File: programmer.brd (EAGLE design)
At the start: 45.7 x 20.3 mm, 23 parts, among them IC1 74241, U1 ATMEGA8U2, X2 SPARKFUN_USB-MICROB, Y1 16MHz

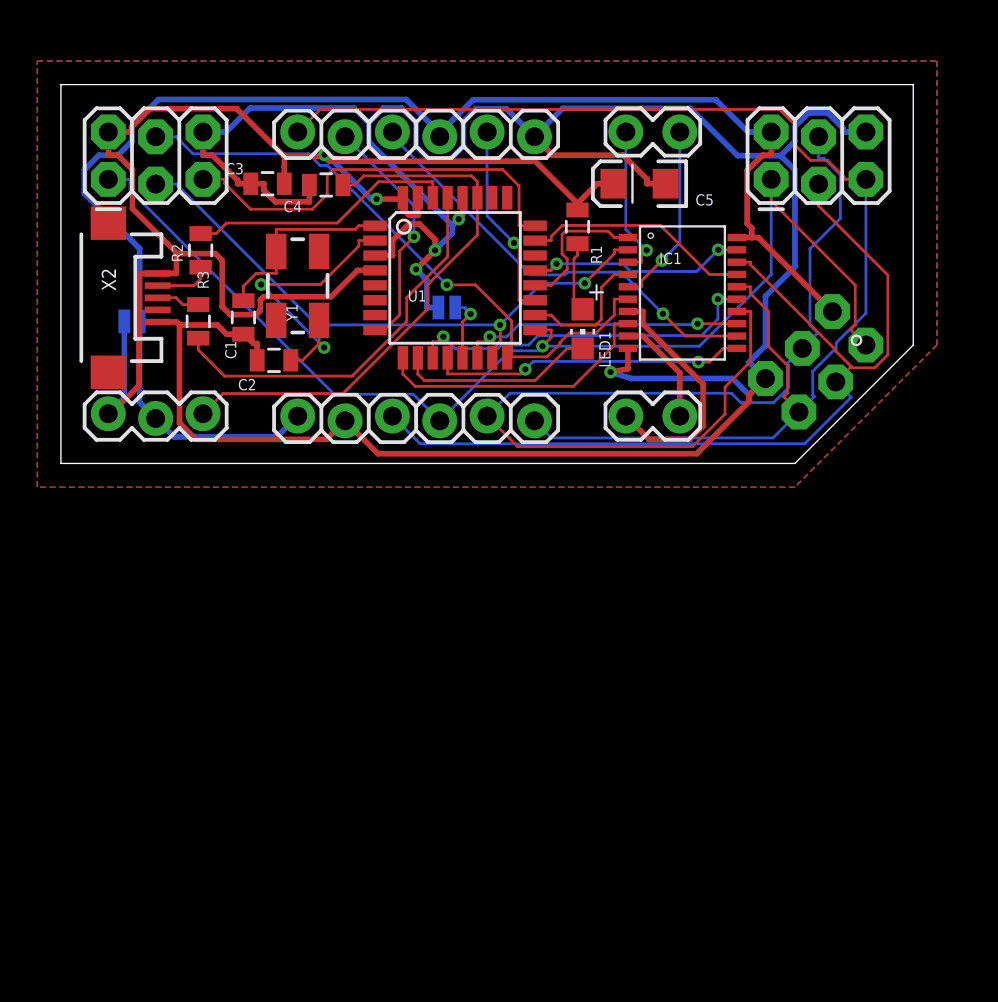
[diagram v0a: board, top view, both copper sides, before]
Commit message: Added gratuitous ground plane vias for more complete coverage.  There was already one (routing, not ground plane) via in a slightly bottom silk-obscuring place, but this change doesn't add any more.
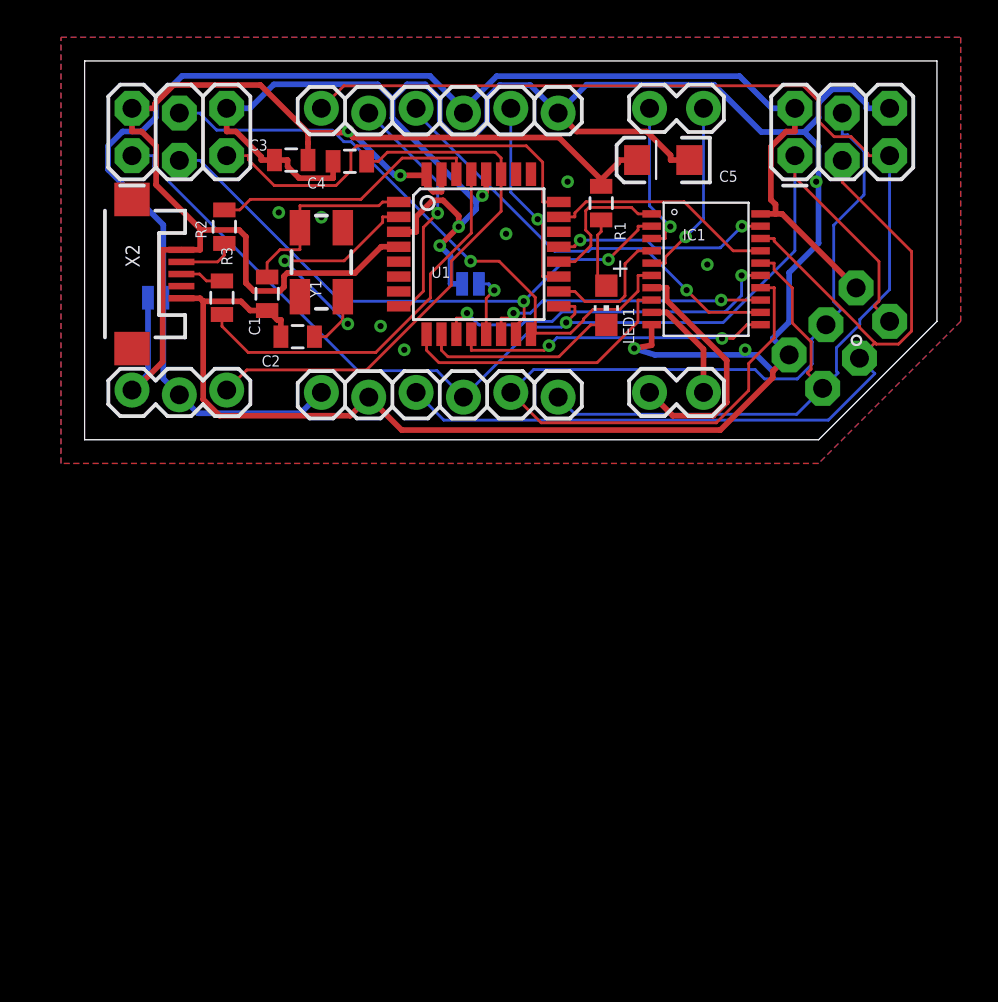
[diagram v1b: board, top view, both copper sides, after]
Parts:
- moved IC1 1.80 mm to (33.4, 9.42)
- moved ISP 1.80 mm to (38.1, 15.2)
- moved ISP-RA 1.80 mm to (43.2, 6.35)
- moved SJ1 1.80 mm to (3.81, 7.62)
- moved X2 1.80 mm to (2.54, 8.89)
- moved JP1 1.80 mm to (2.54, 2.54)
- moved C1 1.80 mm to (9.79, 7.83)
- moved C2 1.80 mm to (11.4, 5.53)
- moved ISP-SELF 1.80 mm to (2.54, 15.2)
- moved JP2 1.80 mm to (12.7, 2.54)
- moved JP5 1.80 mm to (30.5, 2.54)
- moved R2 1.80 mm to (7.49, 11.4)
- moved R3 1.80 mm to (7.37, 7.62)
- moved SJ2 1.80 mm to (20.7, 8.36)
- moved C3 1.80 mm to (11.1, 15.0)
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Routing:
- net GND: vias 4 -> 13

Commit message: Passes design rules now.  More gratuitous ground plane vias, none of which obscure silk.
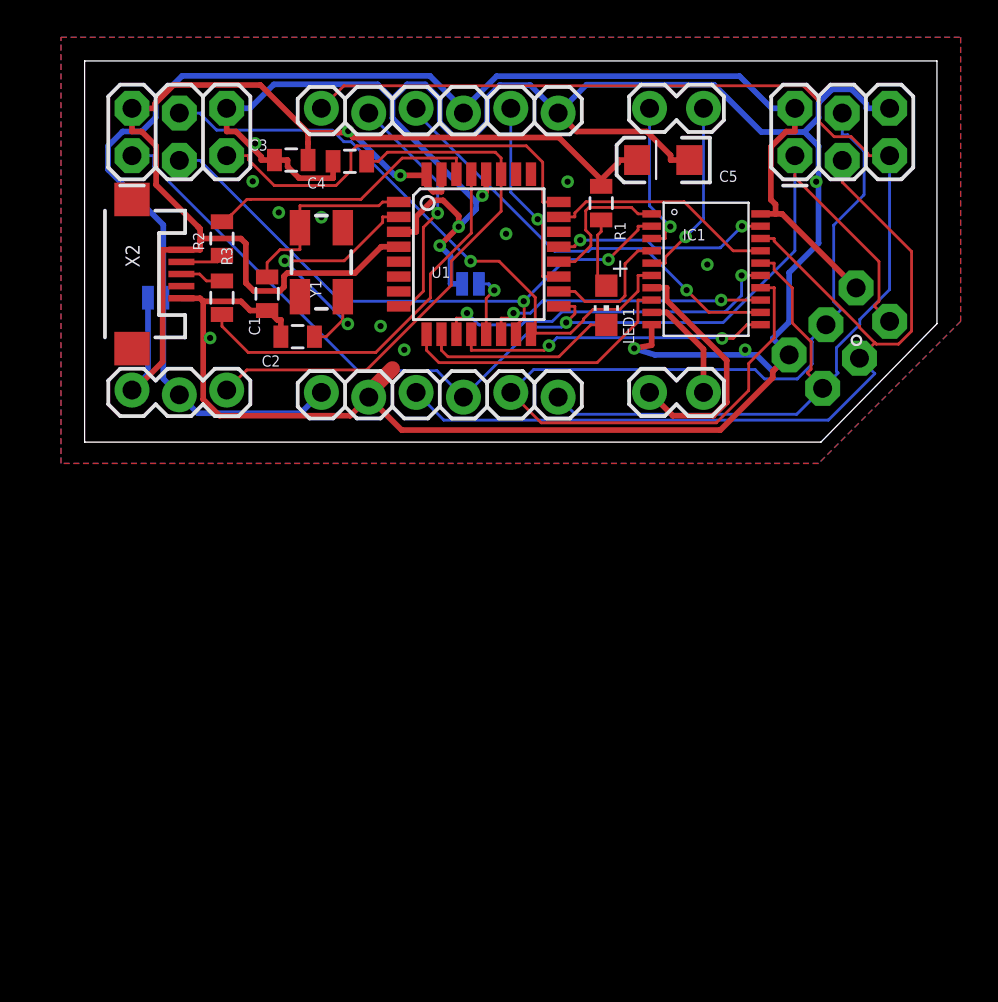
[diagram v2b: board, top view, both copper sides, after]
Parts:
- moved R2 0.65 mm to (7.37, 10.8)
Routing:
- net GND: track 154.3 -> 156.3 mm, vias 13 -> 16
- net D-: track 14.5 -> 16.2 mm
- net D-RAW: track 3.08 -> 2.58 mm
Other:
- board size 45.7 x 20.3 mm -> 45.7 x 20.4 mm
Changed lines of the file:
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@@
 <board>
 <plain>
-<wire x1="0" y1="20.32" x2="0" y2="0" width="0" layer="20"/>
-<wire x1="0" y1="0" x2="39.37" y2="0" width="0" layer="20"/>
-<wire x1="39.37" y1="0" x2="45.72" y2="6.35" width="0" layer="20"/>
-<wire x1="45.72" y1="6.35" x2="45.72" y2="20.32" width="0" layer="20"/>
+<wire x1="0" y1="20.32" x2="0" y2="-0.127" width="0" layer="20"/>
+<wire x1="0" y1="-0.127" x2="39.497" y2="-0.127" width="0" layer="20"/>
+<wire x1="39.497" y1="-0.127" x2="45.72" y2="6.223" width="0" layer="20"/>
+<wire x1="45.72" y1="6.223" x2="45.72" y2="20.32" width="0" layer="20"/>
 <wire x1="45.72" y1="20.32" x2="0" y2="20.32" width="0" layer="20"/>
 <text x="43.18" y="12.065" size="1.27" layer="22" font="vector" rot="MR0">sowbug.com/isp</text>
@@
 <attribute name="VALUE" x="5.8674" y="6.8072" size="0.6" layer="27" font="vector" rot="R270"/>
 </element>
-<element name="R2" library="programmer" package="SPARKFUN_0805" value="22" x="7.493" y="11.43" smashed="yes" rot="R90">
-<attribute name="NAME" x="6.5405" y="10.795" size="0.6" layer="25" font="vector" rot="R90"/>
-<attribute name="VALUE" x="9.0424" y="12.5476" size="0.6" layer="27" font="vector" rot="R90"/>
+<element name="R2" library="programmer" package="SPARKFUN_0805" value="22" x="7.366" y="10.795" smashed="yes" rot="R90">
+<attribute name="NAME" x="6.4135" y="10.16" size="0.6" layer="25" font="vector" rot="R90"/>
+<attribute name="VALUE" x="8.9154" y="11.9126" size="0.6" layer="27" font="vector" rot="R90"/>
 </element>
 <element name="C4" library="programmer" package="SPARKFUN_0805" value="1uF" x="14.2279" y="14.9376" smashed="yes">
@@
 <wire x1="19.627" y1="9.837" x2="19.05" y2="10.414" width="0.3048" layer="16"/>
 <wire x1="19.05" y1="10.414" x2="20.066" y2="11.43" width="0.3048" layer="1"/>
-<polygon width="0.1524" layer="1" isolate="0.254">
+<polygon width="0.3048" layer="1" isolate="0.254">
 <vertex x="-1.27" y="21.59"/>
 <vertex x="46.99" y="21.59"/>
@@
 <vertex x="-1.27" y="-1.27"/>
 </polygon>
-<polygon width="0.1524" layer="16" isolate="0.254">
+<polygon width="0.3048" layer="16" isolate="0.254">
 <vertex x="-1.27" y="21.59"/>
 <vertex x="46.99" y="21.59"/>
@@
 <via x="12.7" y="11.938" extent="1-16" drill="0.3302" diameter="0.6858"/>
 <via x="35.433" y="4.826" extent="1-16" drill="0.3302" diameter="0.6858"/>
+<via x="9.144" y="15.8955" extent="1-16" drill="0.3302" diameter="0.6858"/>
+<via x="9.017" y="13.8635" extent="1-16" drill="0.3302" diameter="0.6858"/>
+<via x="6.731" y="5.461" extent="1-16" drill="0.3302"/>
+<wire x1="39.116" y1="13.97" x2="39.243" y2="13.843" width="0.3048" layer="1"/>
+<wire x1="15.24" y1="2.54" x2="16.51" y2="3.81" width="0.8128" layer="1"/>
 </signal>
 <signal name="D+RAW">
@@
 <contactref element="R2" pad="1"/>
 <contactref element="X2" pad="D-"/>
-<wire x1="7.493" y1="10.53" x2="7.493" y2="9.9013" width="0.1524" layer="1"/>
+<wire x1="7.366" y1="9.895" x2="7.493" y2="9.9013" width="0.1524" layer="1"/>
 <wire x1="5.19" y1="9.54" x2="7.1317" y2="9.54" width="0.1524" layer="1"/>
 <wire x1="7.1317" y1="9.54" x2="7.493" y2="9.9013" width="0.1524" layer="1"/>
@@
 <contactref element="R2" pad="2"/>
 <contactref element="U1" pad="30"/>
-<wire x1="7.493" y1="12.33" x2="8.3217" y2="12.33" width="0.1524" layer="1"/>
 <wire x1="19.9418" y1="14.2472" x2="19.9418" y2="15.1109" width="0.1524" layer="1"/>
 <wire x1="19.9418" y1="15.1109" x2="17.0353" y2="15.1109" width="0.1524" layer="1"/>
 <wire x1="17.0353" y1="15.1109" x2="14.819" y2="12.8946" width="0.1524" layer="1"/>
-<wire x1="14.819" y1="12.8946" x2="8.8863" y2="12.8946" width="0.1524" layer="1"/>
-<wire x1="8.8863" y1="12.8946" x2="8.3217" y2="12.33" width="0.1524" layer="1"/>
+<wire x1="14.819" y1="12.8946" x2="8.89" y2="12.8946" width="0.1524" layer="1"/>
+<wire x1="8.89" y1="12.8946" x2="8.7036" y2="12.8946" width="0.1524" layer="1"/>
+<wire x1="8.7036" y1="12.8946" x2="7.874" y2="12.065" width="0.1524" layer="1"/>
+<wire x1="7.874" y1="12.065" x2="7.493" y2="11.684" width="0.1524" layer="1"/>
+<wire x1="7.366" y1="11.938" x2="7.366" y2="11.695" width="0.1524" layer="1"/>
+<wire x1="7.366" y1="11.695" x2="7.504" y2="11.695" width="0.1524" layer="1"/>
+<wire x1="7.504" y1="11.695" x2="7.874" y2="12.065" width="0.1524" layer="1"/>
+<wire x1="7.874" y1="12.065" x2="7.493" y2="11.684" width="0.1524" layer="1"/>
 </signal>
 <signal name="D+">
@@
 <wire x1="14.4027" y1="16.2144" x2="14.1406" y2="16.4765" width="0.3048" layer="1"/>
 <wire x1="14.1406" y1="16.4765" x2="14.1406" y2="16.5575" width="0.3048" layer="1"/>
-<wire x1="6.2534" y1="11.2534" x2="8.2875" y2="11.2534" width="0.3048" layer="1"/>
-<wire x1="8.2875" y1="11.2534" x2="8.6495" y2="10.8914" width="0.3048" layer="1"/>
-<wire x1="8.6495" y1="10.8914" x2="8.6495" y2="8.4108" width="0.3048" layer="1"/>
 <wire x1="8.6495" y1="8.4108" x2="9.0779" y2="7.9824" width="0.3048" layer="1"/>
 <wire x1="9.0779" y1="7.9824" x2="10.4765" y2="7.9824" width="0.3048" layer="1"/>
@@
 <wire x1="10.8667" y1="8.9422" x2="14.4969" y2="8.9422" width="0.3048" layer="1"/>
 <wire x1="14.4969" y1="8.9422" x2="15.9093" y2="10.3546" width="0.3048" layer="1"/>
-<wire x1="6.1949" y1="10.19" x2="6.1949" y2="11.1949" width="0.3048" layer="1"/>
-<wire x1="6.1949" y1="11.1949" x2="6.2534" y2="11.2534" width="0.3048" layer="1"/>
-<wire x1="6.2534" y1="11.2534" x2="3.8352" y2="13.6716" width="0.3048" layer="1"/>
+<wire x1="6.1949" y1="10.19" x2="6.1949" y2="10.668" width="0.3048" layer="1"/>
+<wire x1="6.1949" y1="10.668" x2="6.1949" y2="11.3219" width="0.3048" layer="1"/>
+<wire x1="6.1264" y1="11.3804" x2="6.0864" y2="11.4204" width="0.3048" layer="1"/>
+<wire x1="6.0864" y1="11.4204" x2="3.8352" y2="13.6716" width="0.3048" layer="1"/>
 <wire x1="3.8352" y1="13.6716" x2="3.8352" y2="15.7559" width="0.3048" layer="1"/>
 <wire x1="3.8352" y1="15.7559" x2="3.0558" y2="16.5353" width="0.3048" layer="1"/>
@@
 <wire x1="4.1851" y1="4.18" x2="2.6721" y2="2.667" width="0.3048" layer="1"/>
 <wire x1="2.6721" y1="2.667" x2="2.54" y2="2.667" width="0.3048" layer="1"/>
+<wire x1="8.6495" y1="8.4108" x2="8.6495" y2="10.5275" width="0.3048" layer="1"/>
+<wire x1="8.6495" y1="10.5275" x2="8.382" y2="10.795" width="0.3048" layer="1"/>
+<wire x1="8.382" y1="10.795" x2="6.3219" y2="10.795" width="0.3048" layer="1"/>
+<wire x1="6.3219" y1="10.795" x2="6.1949" y2="10.668" width="0.3048" layer="1"/>
+<wire x1="6.096" y1="11.43" x2="6.1949" y2="11.3219" width="0.3048" layer="1"/>
+<wire x1="6.096" y1="11.43" x2="6.0864" y2="11.4204" width="0.3048" layer="1"/>
 </signal>
 <signal name="RST/TMS/DTR-B">

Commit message: 8 mil traces and vias = cheaper fab
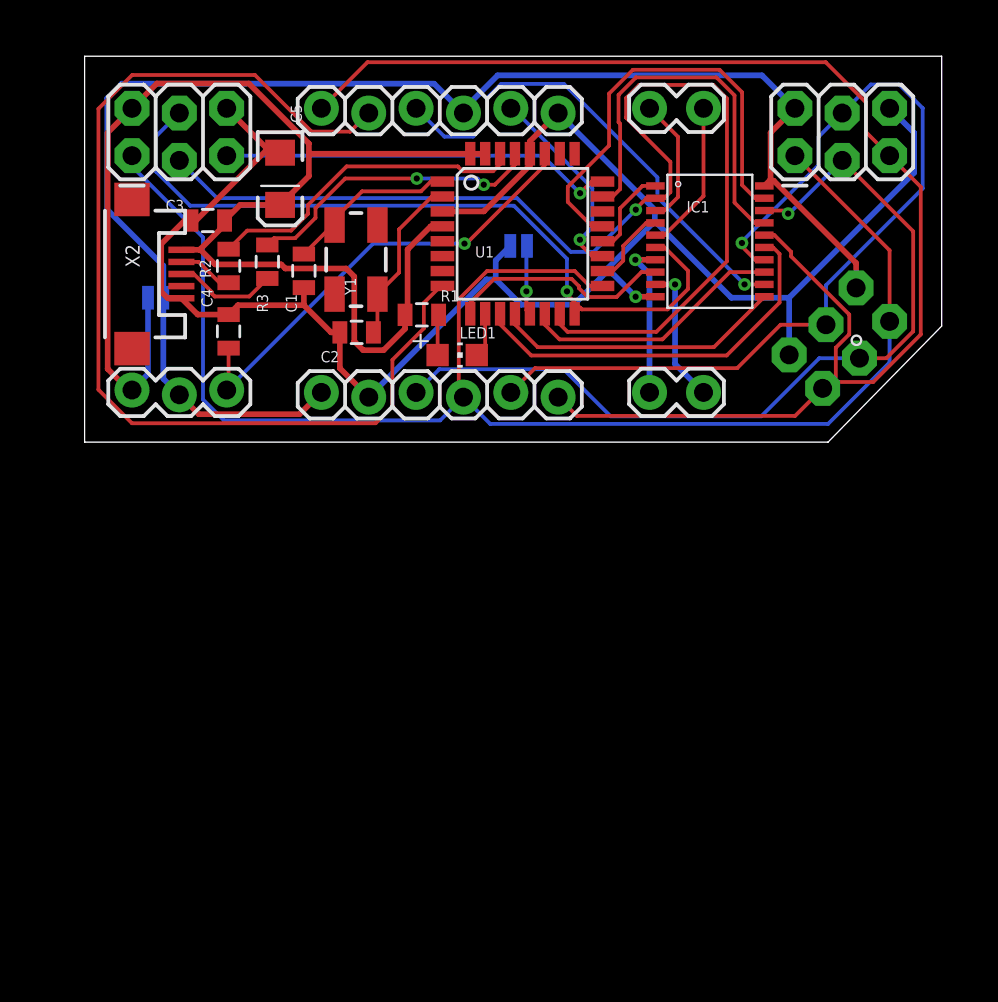
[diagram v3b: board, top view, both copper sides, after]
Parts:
- moved C5 20.6 mm to (10.5, 14.0), turned to 270 degrees
- moved R1 11.3 mm to (18.1, 6.70), turned to 180 degrees
- moved C4 11.2 mm to (7.72, 5.82), turned to 270 degrees
- moved LED1 8.44 mm to (20.0, 4.54), turned to 270 degrees
- moved C3 5.53 mm to (6.61, 11.8)
- moved SJ2 3.29 mm to (23.3, 10.4)
- moved C2 3.17 mm to (14.6, 5.76)
- moved R3 3.11 mm to (9.80, 9.55), turned to 90 degrees
- moved U1 2.59 mm to (23.5, 11.1)
- moved C1 2.32 mm to (11.8, 9.06)
- moved Y1 1.86 mm to (14.6, 9.66)
- moved R2 1.51 mm to (7.72, 9.32)
- moved IC1 1.51 mm to (33.6, 10.9)
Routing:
- net GND: track 156.3 -> 98.4 mm, vias 16 -> 1
- net RXI: track 13.1 -> 56.5 mm, vias 1 -> 0
- net SCK/TCK: track 32.3 -> 61.7 mm, vias 2 -> 1
- net MISO/TDO: track 62.8 -> 81.6 mm, vias 1 -> 0
- net BUFFER-OE2: track 11.7 -> 23.8 mm, vias 2 -> 0
- net ECLK: track 12.4 -> 21.0 mm
- net ACTIVITY: track 10.6 -> 2.40 mm
- net MOSI/TDI: track 33.5 -> 40.5 mm
- net XTAL2: track 15.5 -> 9.15 mm, vias 2 -> 0
- net RST/TMS/DTR-B: track 71.3 -> 76.9 mm
- net MOSI/TDI-B: track 54.1 -> 48.5 mm, vias 0 -> 1
- net D+: track 21.1 -> 16.2 mm, vias 0 -> 2
- net 3.3V: track 29.9 -> 25.0 mm, vias 0 -> 1
- net PB0-B: track 13.2 -> 8.51 mm, vias 0 -> 1
- net SCK/TCK-B: track 50.6 -> 46.3 mm, vias 0 -> 1
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- removed copper zone on layer 1, net GND
- removed copper zone on layer 16, net GND
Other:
- board size 45.7 x 20.4 mm -> 46 x 20.7 mm

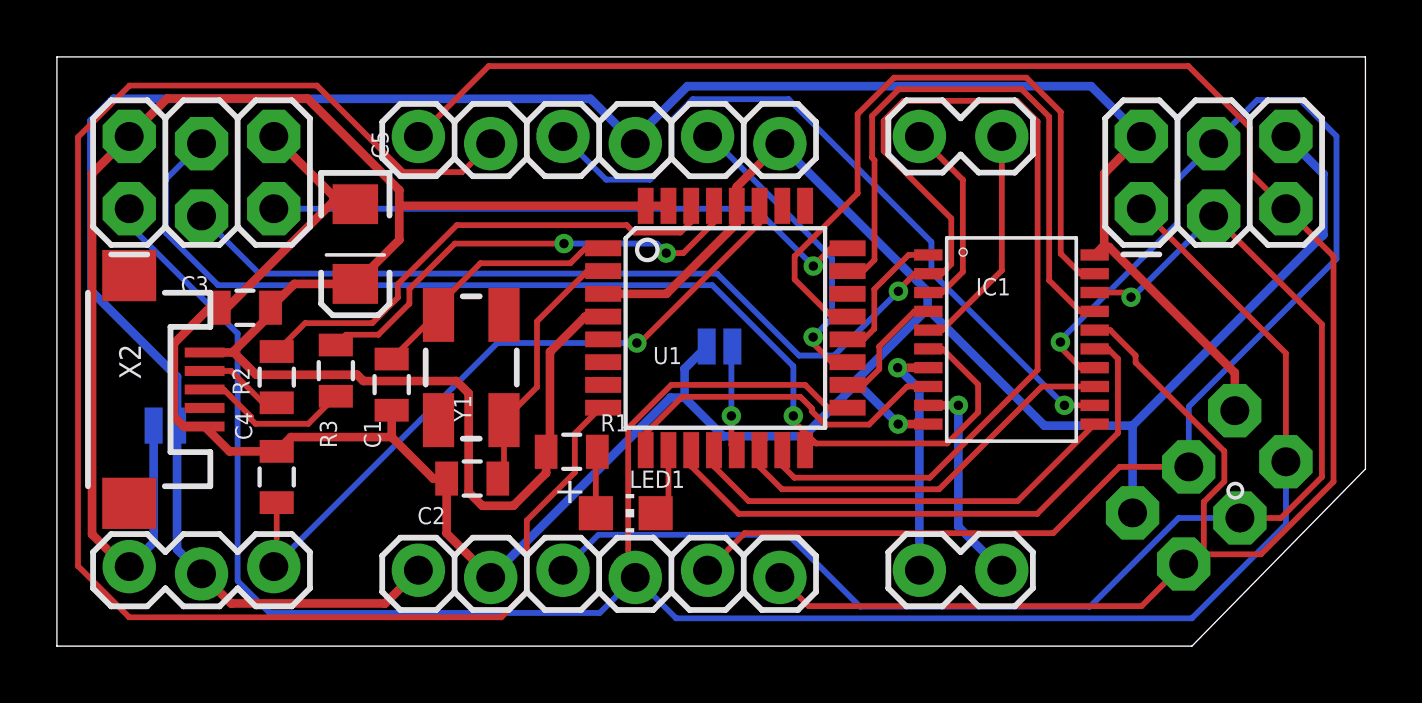
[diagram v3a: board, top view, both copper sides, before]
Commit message: 8 mil, reasonable routing.
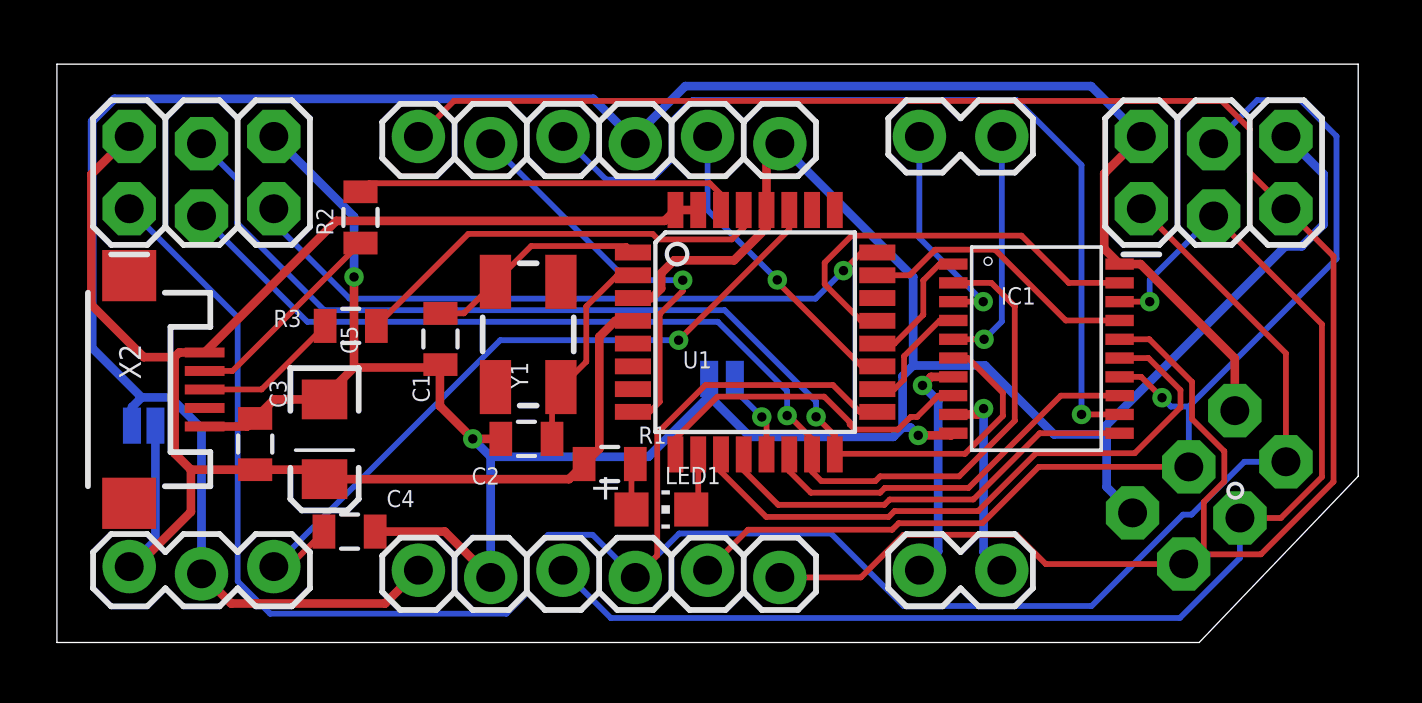
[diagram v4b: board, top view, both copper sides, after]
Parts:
- moved C5 6.94 mm to (9.40, 7.14)
- moved R2 6.34 mm to (10.7, 14.9)
- moved C3 4.80 mm to (6.97, 6.97), turned to 90 degrees
- moved C4 3.20 mm to (10.3, 3.90), turned to 180 degrees
- moved C2 2.36 mm to (16.5, 7.15)
- moved C1 2.35 mm to (13.5, 10.7)
- moved Y1 2.31 mm to (16.6, 10.8)
- moved R3 1.66 mm to (10.3, 11.1), turned to 0 degrees
- moved R1 1.40 mm to (19.4, 6.27)
- moved LED1 1.26 mm to (21.2, 4.67)
- moved SJ2 1.14 mm to (23.4, 9.26)
- moved U1 1.06 mm to (24.5, 10.9)
- moved IC1 0.93 mm to (34.4, 10.6)
- moved SJ1 0.76 mm to (3.05, 7.62), turned to 0 degrees
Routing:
- net RXI: track 56.5 -> 14.4 mm, vias 0 -> 1
- net SCK/TCK: track 61.7 -> 41.0 mm
- net ECLK: track 21.0 -> 9.91 mm
- net 5V: track 75.2 -> 64.9 mm
- net BUFFER-OE2: track 23.8 -> 14.6 mm
- net MOSI/TDI-B: track 48.5 -> 40.5 mm
- net TXO-B: track 26.3 -> 31.8 mm
- net D-RAW: track 3.00 -> 7.34 mm
- net D-: track 17.5 -> 13.5 mm
- net MOSI/TDI: track 40.5 -> 37.9 mm
- net /RESET: track 21.3 -> 23.5 mm
- net XTAL2: track 9.15 -> 7.25 mm
- net XTAL1: track 9.74 -> 7.84 mm
- net MISO/TDO: track 81.6 -> 83.5 mm
- net VCC: track 78.2 -> 79.7 mm
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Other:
- board size 46 x 20.7 mm -> 45.7 x 20.3 mm
